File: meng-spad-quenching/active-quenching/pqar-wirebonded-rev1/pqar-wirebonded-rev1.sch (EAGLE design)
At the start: 62 parts, among them IC1 NL17SZ125, IC2 LTC1711, IC20 NC7WZ16P6X, IC3 NC7SV74K8X, IC4 BCV62, IC5 74AHC1G14DCK, IC6 SPAD, IC7 74AUC1G32DCK, IC8 74LVC1G02DCK, U1 SN74LVC1G123DCUT, X1 V_A, X2 OUT, X3 V_LOGIC, X4 I_HOLDOFF, X5 FORCE_QUENCH

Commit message: Cleaned stop mask errors on silkscreen
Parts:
- removed TP3: AV_DET, testpad:TPTP10R
- added TP2: AV_DET, testpad:TPTP10R
- C1: value CAP CER 100PF 50V C0G 0603 5% -> IPDiA 935131425610
- C10, C16: value IPDiA 935131425610 -> DNP; device rcl-modified-footprints:C-EUC0603 -> rcl-modified-footprints:C-EUC0805
- C11: value IPDiA 935131425610 -> CAP CER 0.1UF 50V X7R 0805 5%; device rcl-modified-footprints:C-EUC0603 -> rcl-modified-footprints:C-EUC0805
- C13, C14: value DNP -> CAP CER 0.1UF 50V X7R 0805 5%
- C15: value CAP CER 0.1UF 50V X7R 0603 5% -> IPDiA 935131425610
- C17, C2, C5: value CAP CER 0.1UF 50V X7R 0805 5% -> CAP CER 0.1UF 50V X7R 0603 5%; device rcl-modified-footprints:C-EUC0805 -> rcl-modified-footprints:C-EUC0603
- C18: value CAP CER 0.1UF 50V X7R 0603 5% -> DNP; device rcl-modified-footprints:C-EUC0603 -> rcl-modified-footprints:C-EUC0805
- C3: value CAP CER 0.1UF 50V X7R 0603 5% -> CAP CER 100PF 50V C0G 0603 5%
- C8: value DNP -> IPDiA 935131425610; device rcl-modified-footprints:C-EUC0805 -> rcl-modified-footprints:C-EUC0603
- IC1: value NL17SZ125 -> SPAD; device 74xx-little-de:74AHC1G125DCK -> meng:SPAD-GENERIC
- IC2: value LTC1711 -> NL17SZ125; device meng:LTC1711 -> 74xx-little-de:74AHC1G125DCK
- IC3: value NC7SV74K8X -> 74AUC1G32DCK; device meng:NC7SV74K8X -> 74xx-little-us:74AUC1G32DCK
- IC5: value 74AHC1G14DCK -> NC7SV74K8X; device 74xx-little-us:74AHC1G14DCK -> meng:NC7SV74K8X
- IC6: value SPAD -> 74AHC1G14DCK; device meng:SPAD-GENERIC -> 74xx-little-us:74AHC1G14DCK
- IC7: value 74AUC1G32DCK -> 74LVC1G02DCK; device 74xx-little-us:74AUC1G32DCK -> 74xx-little-us:74LVC1G02DCK
- IC8: value 74LVC1G02DCK -> LTC1711; device 74xx-little-us:74LVC1G02DCK -> meng:LTC1711
- R1: value RES SMD 10M OHM 1% 1/10W 0603 -> DNP; device rcl-modified-footprints:R-EU_R0603 -> rcl-modified-footprints:R-EU_R0805
- R10: value DNP -> RES SMD 0R 0603; device rcl-modified-footprints:R-EU_R0805 -> rcl-modified-footprints:R-EU_R0603
- R11: value RES SMD 0R 0603 -> RES SMD 1K OHM 1% 1/10W 0603
- R12: value RES SMD 0R 0805 -> RES SMD 1K OHM 1% 1/10W 0603; device rcl-modified-footprints:R-EU_R0805 -> rcl-modified-footprints:R-EU_R0603
- R14, R16: value DNP -> RES SMD 0R 0805; device rcl-modified-footprints:R-EU_R0603 -> rcl-modified-footprints:R-EU_R0805
- R15: value RES SMD 10K OHM 1% 1/10W 0603 -> DNP; device rcl-modified-footprints:R-EU_R0603 -> rcl-modified-footprints:R-EU_R0805
- R17: value RES SMD 0R 0805 -> RES SMD 10K OHM 1% 1/10W 0603; device rcl-modified-footprints:R-EU_R0805 -> rcl-modified-footprints:R-EU_R0603
- R2: value RES SMD 1K OHM 1% 1/10W 0805 -> DNP
- R3: value RES SMD 1K OHM 1% 1/10W 0603 -> DNP
- R6: value RES SMD 1K OHM 1% 1/10W 0603 -> DNP; device rcl-modified-footprints:R-EU_R0603 -> rcl-modified-footprints:R-EU_R0805
- R7: value DNP -> RES SMD 1K OHM 1% 1/10W 0805
- R8: value DNP -> RES SMD 10M OHM 1% 1/10W 0603; device rcl-modified-footprints:R-EU_R0805 -> rcl-modified-footprints:R-EU_R0603
- R9: device rcl-modified-footprints:R-EU_R0805 -> rcl-modified-footprints:R-EU_R0603
- X1: value V_A -> I_HOLDOFF
- X2: value OUT -> V_LOGIC
- X3: value V_LOGIC -> FORCE_QUENCH
- X4: value I_HOLDOFF -> OUT
- X5: value FORCE_QUENCH -> V_A
- renumbered IC20 to IC9, R52 to R18
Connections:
- net !AV_DET: now also C16.2, IC8.!Q, R1.1, TP1.TP; no longer C14.2, IC2.!Q, R9.1, TP3.TP
- net !EN_DRIVER: now also IC2A.OE, IC7A.O; no longer IC1A.OE, IC8A.O
- net !QUENCH: now also IC6A.O, R10.2; no longer IC5A.O, R11.2
- net !RESET: now also IC5.!Q, R14.1; no longer IC3.!Q, R12.1
- net !RESET_RC: now also C10.1, IC5.!CLR, R14.2; no longer C8.1, IC3.!CLR, R12.2
- net +5V: now also C1.1, C15.1, C17.1, C2.1, C5.1, C8.1, IC2P.VCC, IC3P.VCC, IC5.!PRE, IC5.D, IC5.VDD, IC6P.VCC, L2.P$1, L5.P$2, R15.1; no longer C10.1, C11.1, C16.1, C18.1, C4.1, C6.1, IC1P.VCC, IC3.!PRE, IC3.D, IC3.VDD, IC5P.VCC, IC8P.VCC, L1.P$2, L5.P$1, R10.1
- net ANODE: now also IC1.SPAD_ANODE, IC2A.O, R8.1; no longer IC1A.O, IC6.SPAD_ANODE, R1.1
- net AV_DET: now also C18.2, IC8.Q, R2.1, TP2.TP; no longer C13.2, IC2.Q, R8.1, TP1.TP
- net AV_DET_REF: now also C18.1, IC8.+IN, R11.1, R12.2; no longer C13.1, IC2.+IN, R5.2, R6.1
- net CEXT: now also C11.2; no longer C5.2
- net CLK_RESET: now also IC5.CLK, R1.2, R10.1, R16.1, R2.2, R3.1; no longer IC3.CLK, R11.1, R14.1, R17.1, R8.2, R9.2
- net CLK_RESET_JUMP: now also R16.2; no longer R17.2
- net DRIVER_IN: now also IC2A.I, IC7A.I0, R6.1; no longer IC1A.I, IC8A.I0, R7.1
- net FORCE_QUENCH: now also IC3A.I1, R17.1, X3C.1; no longer IC7A.I1, R15.1, X5C.1
- net GND: now also C1.2, C13.2, C14.2, C5.2, IC1.GND, IC2P.GND, IC3P.GND, IC5.GND, IC6P.GND, IC8.GND, IC8.LEN, IC8.V-, R11.2, R17.2, R8.2; no longer C11.2, C16.2, C18.2, C3.2, IC1P.GND, IC2.GND, IC2.LEN, IC2.V-, IC3.GND, IC5P.GND, IC6.GND, IC8P.GND, R1.2, R15.2, R7.2
- net HOLDOFF_CAP: now also C11.1, R15.2; no longer C5.1, R10.2
- net HOLDOFF_TIMER: now also IC3A.I0, R9.2; no longer IC7A.I0, R16.2
- net I_HOLDOFF: now also L1.P$1, X1C.1; no longer L2.P$1, X4C.1
- net I_HOLDOFF_FILT: now also C4.1, L1.P$2; no longer C15.1, L2.P$2
- net KATHODE: now also C3.1, IC1.SPAD_CATHODE, R7.2; no longer C1.1, IC6.SPAD_CATHODE, R2.2
- net KATHODE_C: now also C16.1, C3.2, IC8.-IN, R5.2; no longer C1.2, C14.1, IC2.-IN, R3.2
- net OUT_R: now also X4C.1; no longer X2C.1
- net QUENCH: now also IC3A.O, IC6A.I, R3.2, R9.1; no longer IC5A.I, IC7A.O, R14.2, R16.1
- net RESET: now also IC5.Q, IC7A.I1; no longer IC3.Q, IC8A.I1
- net VDD_COMP: now also C6.1, IC8.V+, L3.P$2, R12.1; no longer C3.1, IC2.V+, L4.P$2, R3.1
- net VDD_COMP_JUMP: now also L2.P$2, L3.P$1; no longer L4.P$1, L5.P$2
- net V_A: now also C14.1, L4.P$1, X5C.1; no longer C17.1, L3.P$1, X1C.1
- net V_A_FILT: now also C13.1, L4.P$2, R7.1; no longer C2.1, L3.P$2, R2.1
- net V_LOGIC: now also L5.P$1, X2C.1; no longer L1.P$1, X3C.1
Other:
- moved on the sheet: C1, C10, C11, C12, C13, C14, C15, C16, C17, C18, C2, C3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

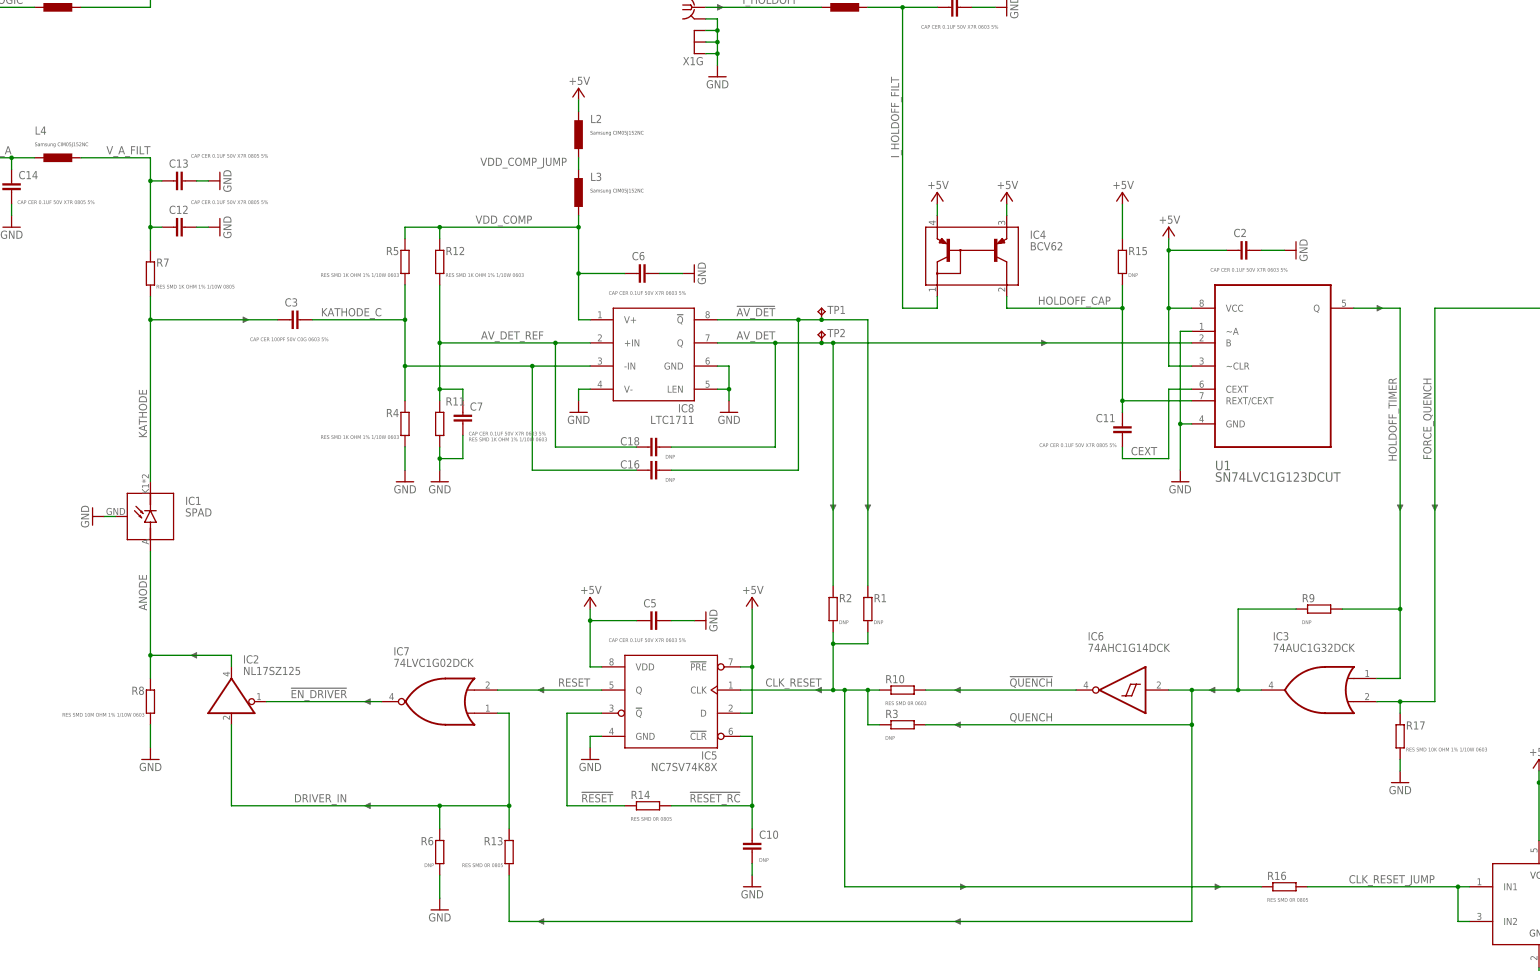
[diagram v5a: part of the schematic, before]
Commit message: Add wirebonding pads for substrate bias
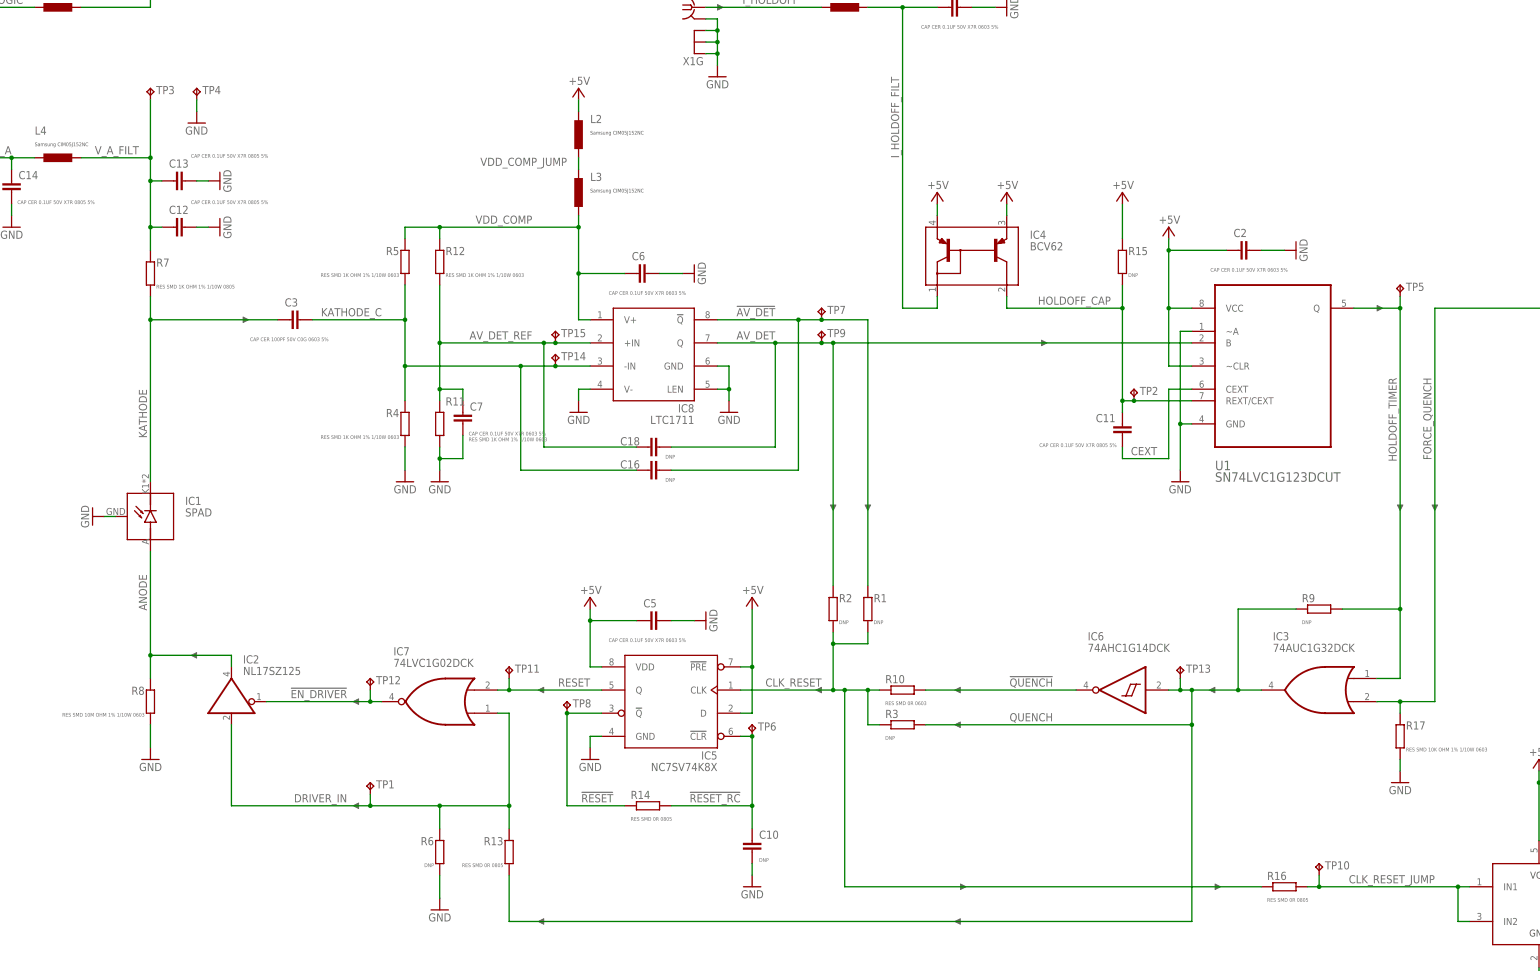
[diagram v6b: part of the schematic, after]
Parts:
- added TP10, TP11, TP12, TP13, TP14, TP15, TP3, TP4, TP5, TP6, TP7, TP8, TP9: AV_DET, testpad:TPTP10R
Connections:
- net !AV_DET: now also TP7.TP; no longer TP1.TP
- net !EN_DRIVER: now also TP12.TP
- net !RESET: now also TP8.TP
- net !RESET_RC: now also TP6.TP
- net AV_DET: now also TP9.TP; no longer TP2.TP
- net AV_DET_REF: now also TP15.TP
- net CLK_RESET_JUMP: now also TP10.TP
- net DRIVER_IN: now also TP1.TP
- net GND: now also TP4.TP
- net HOLDOFF_CAP: now also TP2.TP
- net HOLDOFF_TIMER: now also TP5.TP
- net KATHODE_C: now also TP14.TP
- net QUENCH: now also TP13.TP
- net RESET: now also TP11.TP
- net V_A_FILT: now also TP3.TP
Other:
- moved on the sheet: TP1, TP2

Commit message: Created BOM
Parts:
- C1, C15, C8, C9: value IPDiA 935131425610 -> CAP CER 0.1UF 50V X7R 0603 5%
- C11: value CAP CER 0.1UF 50V X7R 0805 5% -> CAP FILM 100PF 5% 0805
- C7: value CAP CER 0.1UF 50V X7R 0603 5% -> DNP
- IC2: value NL17SZ125 -> NL17SZ125DFT2G
- IC3: value 74AUC1G32DCK -> NL17SZ32DFT2G
- IC6: value 74AHC1G14DCK -> NL17SZ14DFT2G
- IC7: value 74LVC1G02DCK -> NL17SZ02DFT2G
- IC8: value LTC1711 -> LT1711
- L1, L2, L3, L4, L5: value Samsung CIM05J152NC -> FERRITE BEAD 1.5 KOHM 0402 1LN
- R11, R5: value RES SMD 1K OHM 1% 1/10W 0603 -> RES SMD 10.2K OHM 1% 1/10W 0603
- R12, R4: value RES SMD 1K OHM 1% 1/10W 0603 -> RES SMD 10K OHM 1% 1/10W 0603
- R18: value RES SMD 49.9 OHM 1% 1/10W 0805 -> RES SMD 49.9 OHM 1% 1/8W 0805
- R8: value RES SMD 10M OHM 1% 1/10W 0603 -> RES SMD 10M OHM 5% 1/10W 0603
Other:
- note added: "Use as back-termination Do not terminate load to reduce IIR Or, put in 0R"
- note added: "tpd=2.3ns @ 5V"
- moved on the sheet: C14, L4, L5, X2C, X2G, X5C, X5G
